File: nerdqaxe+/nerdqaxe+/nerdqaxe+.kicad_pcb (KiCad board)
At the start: 4 copper layers, 89 x 152 mm, 206 parts, among them J1 Barrel_Jack_Switch, J2 Conn_01x06, M1 Fan_4pin, M2 Fan_4pin, U19 BM1368_mode1, U20 BM1368_mode1, U25 BM1368_mode1, U26 BM1368_mode1, U3 TPS53647, U30 T-Display-S3, U32 EMC2302-1, U33 TXU0102-DCU, U35 TXU0304PW, U36 MCP1824T-1802E, U37 TMP1075, U38 TMP1075, U4 CSD95472Q5MC, U5 CSD95472Q5MC, U6 AP3211, U7 MCP1824T-0802E, U8 25MHz

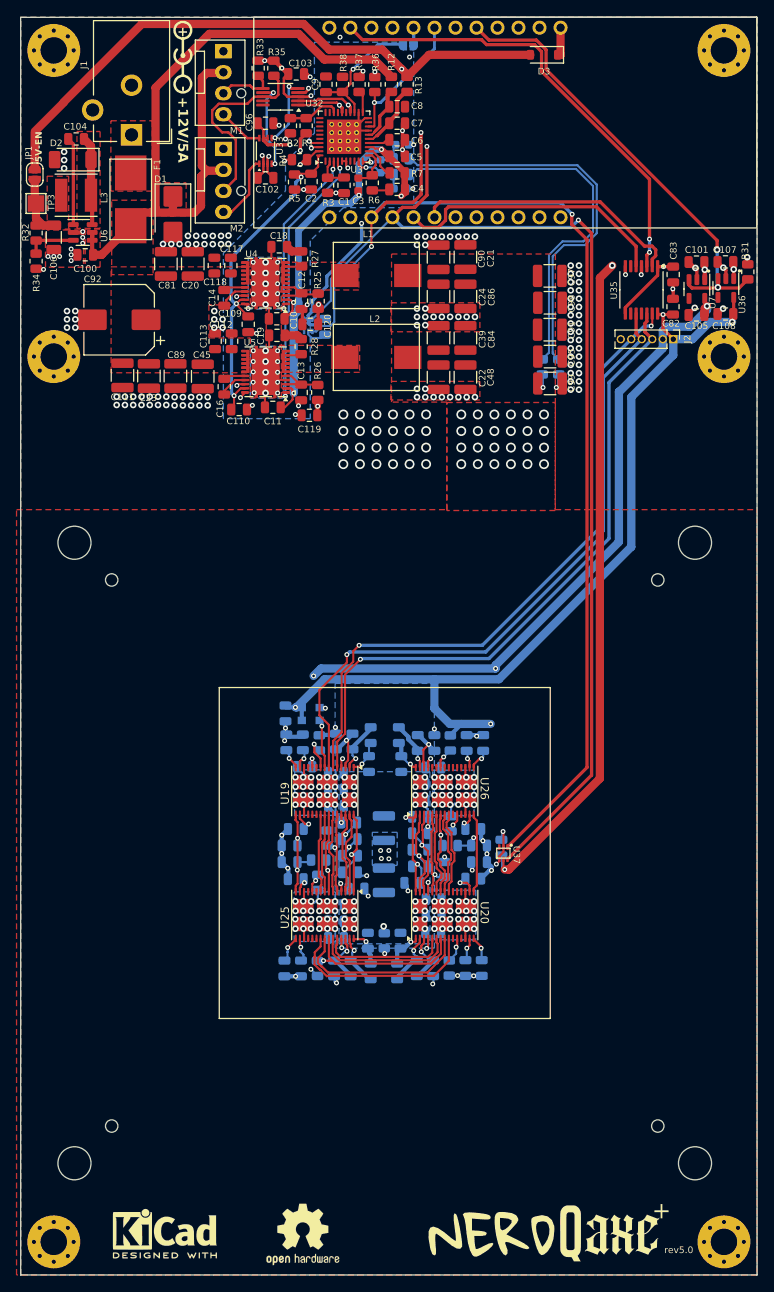
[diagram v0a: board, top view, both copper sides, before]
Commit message: switched to 6 layer, lga1700 instead of lga115x holes
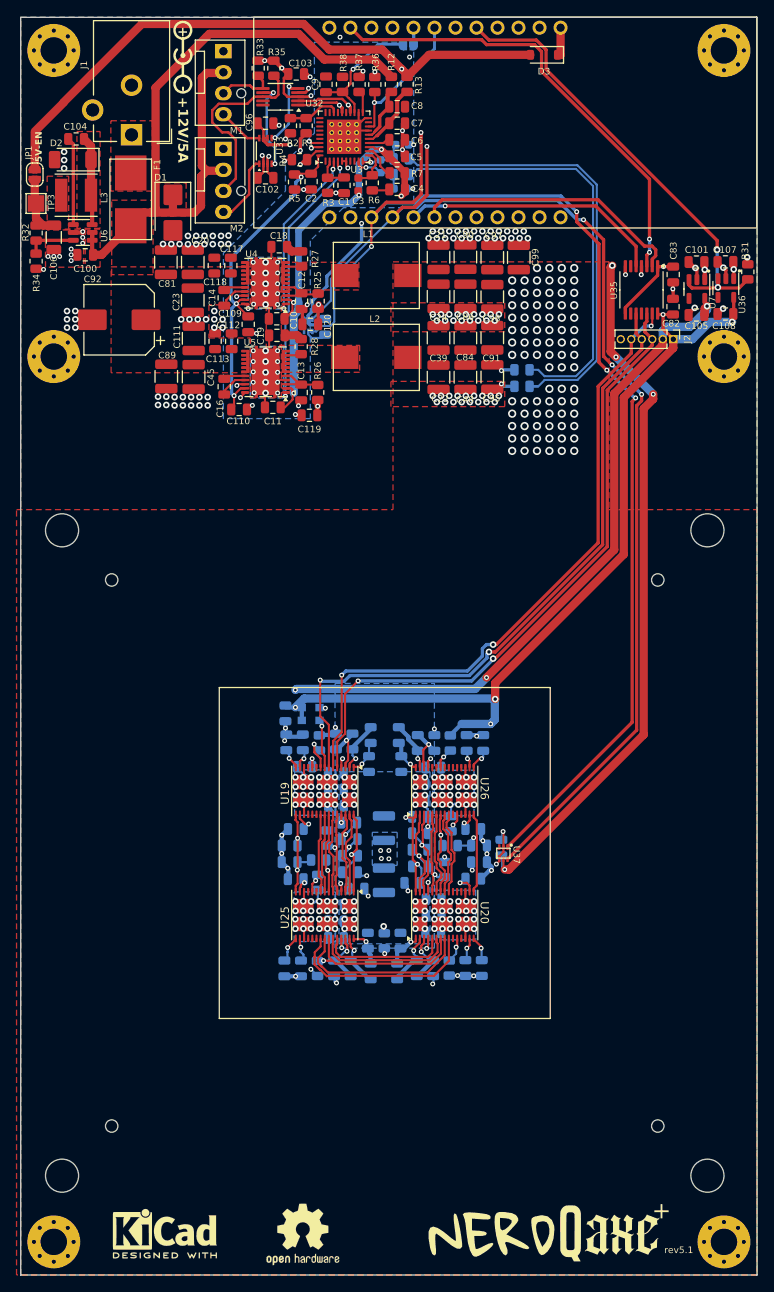
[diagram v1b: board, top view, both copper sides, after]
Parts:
- moved C99 15.7 mm to (111.2, 53.0), turned to 90 degrees
- moved C23 10.6 mm to (71.8, 58.2)
- moved C111 9.69 mm to (71.9, 62.8), turned to 90 degrees
- moved C95 7.40 mm to (108.0, 67.5), turned to -90 degrees
- moved C97 7.30 mm to (108.0, 53.0), turned to 90 degrees
- moved C91 7.02 mm to (108.0, 62.7), turned to 90 degrees
- moved C98 7.01 mm to (108.0, 57.8), turned to -90 degrees
- moved R30 5.03 mm to (111.6, 68.6), turned to 180 degrees
- moved R29 2.47 mm to (111.6, 66.6), turned to 180 degrees
- moved REF** 1.50 mm to (132.5, 86.0)
- moved C89 1.10 mm to (68.6, 67.4)
- moved C45 1.10 mm to (71.9, 67.5)
- moved C20 0.20 mm to (71.8, 53.6)
- moved C81 0.20 mm to (68.5, 53.6)
- moved D1 0.20 mm to (69.4, 47.6)
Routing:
- net /Power/VSENSE-: track 49.1 -> 55.9 mm
- net /T-Display-S3/SDA: track 151.9 -> 158.2 mm, vias 3 -> 5
- net /T-Display-S3/SCL: track 156.8 -> 162.8 mm, vias 4 -> 6
- net /Power/VSENSE+: track 48.4 -> 53.2 mm
- net +3V3: track 129.2 -> 133.4 mm, vias 13 -> 15
- net +1V8: track 214.6 -> 211.4 mm, vias 13 -> 14
- net /BM1366/RXD: track 33.6 -> 31.9 mm, vias 0 -> 1
- net /BM1366/RO: track 81.3 -> 82.4 mm, vias 1 -> 2
- net /BM1366/RST_N: track 80.1 -> 79.2 mm, vias 1 -> 2
- net /BM1366/CI: track 80.0 -> 80.5 mm, vias 2 -> 3
- net GND: vias 338 -> 303
- net +1V2: vias 60 -> 118
- added copper zone on In2.Cu, net +1V2
- added copper zone on In3.Cu, net +1V2
- added copper zone on In4.Cu, net +1V2
- added copper zone on In3.Cu, net GND
- added copper zone on In4.Cu, net GND
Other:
- copper layers 4 -> 6
- board text added: "rev5.1"
- board text removed: "rev5.0"
